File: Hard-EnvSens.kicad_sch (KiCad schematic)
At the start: 58 parts, among them J1 TYPE-C-31-M-12, J2 Conn_01x04_Socket, J3 Conn_02x02_Odd_Even, J4 Conn_01x04_Pin, Q1 SS8050, Q2 SS8050, SW1 SW_Push, SW3 SW_Push, U1 LD1117S33TR_SOT223, U2 ESP32-C6-WROOM-1, U4 VEML7700-TR, U5 DPS368, U6 SGP41-D-R4, U7 SHT40-AD1B-R2, U8 AS7341-DLGT, U9 TPS79318DBVTG4

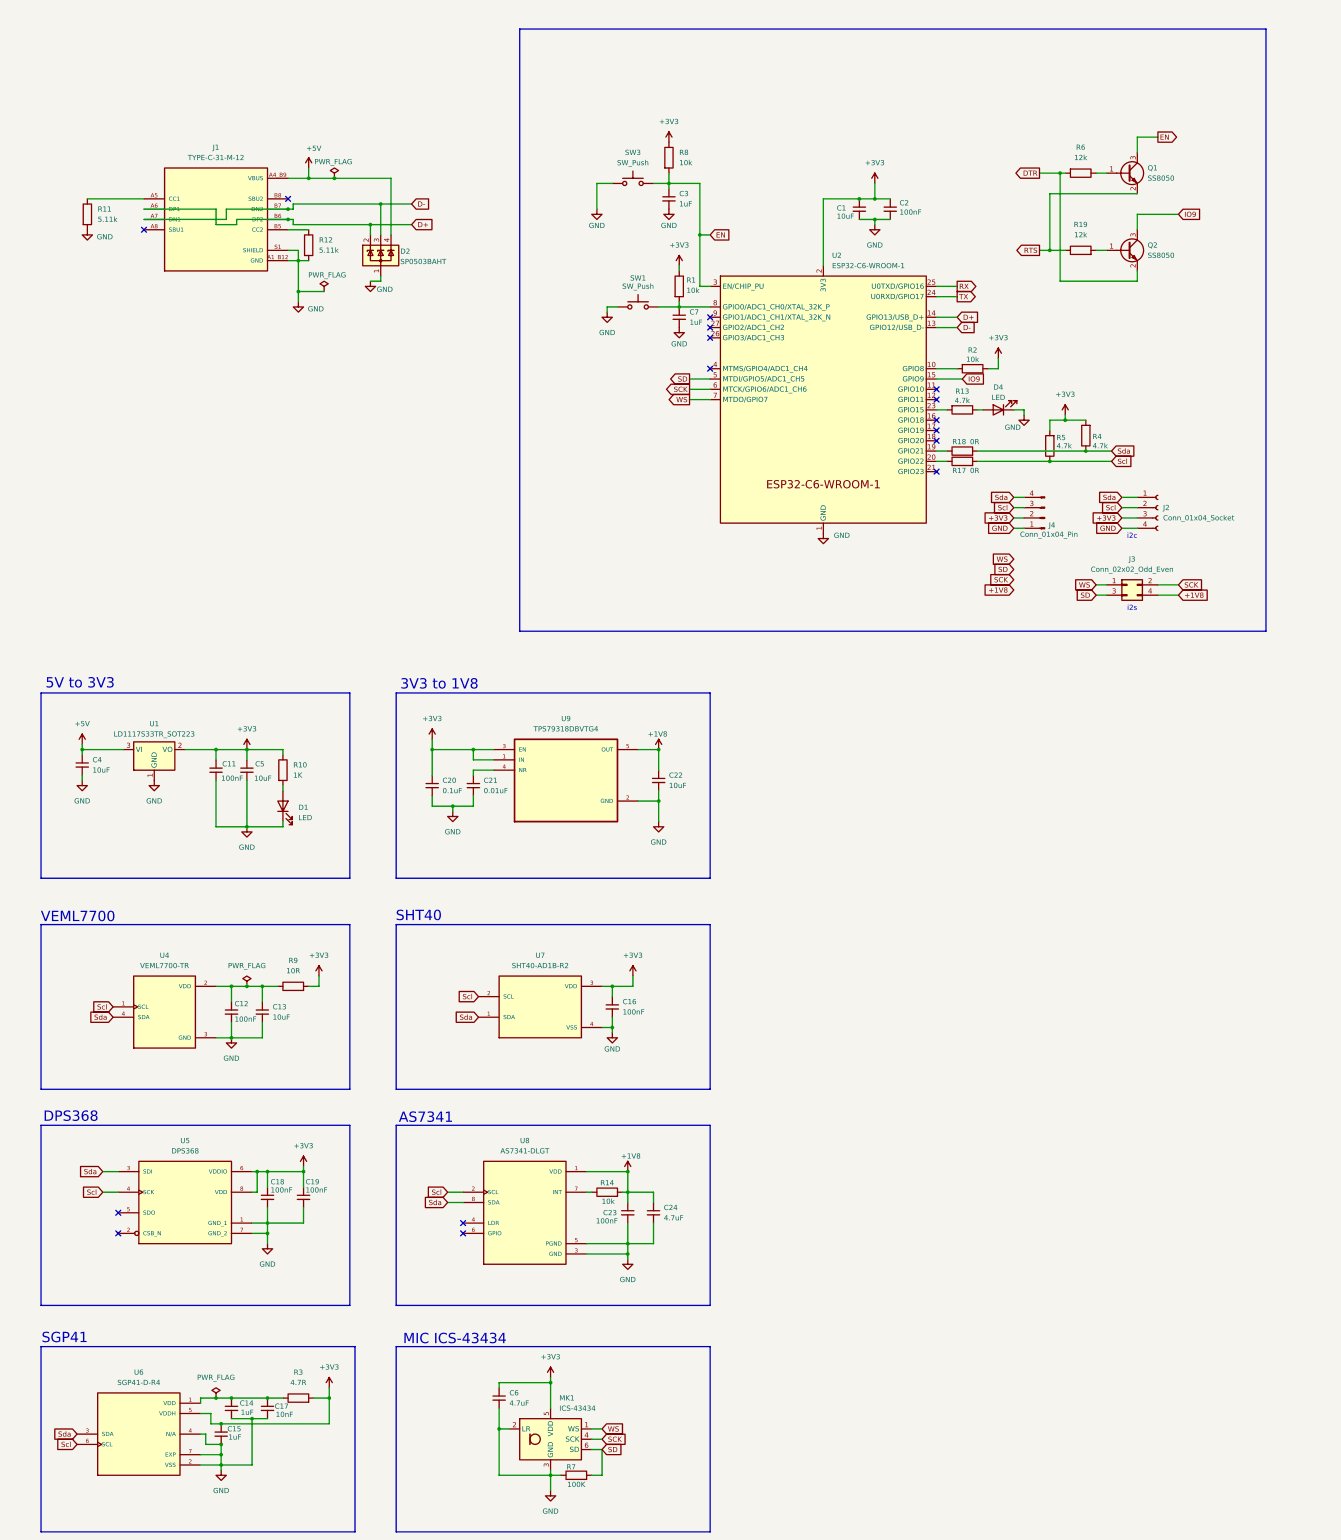
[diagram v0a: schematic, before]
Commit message: Full connected board, no charger
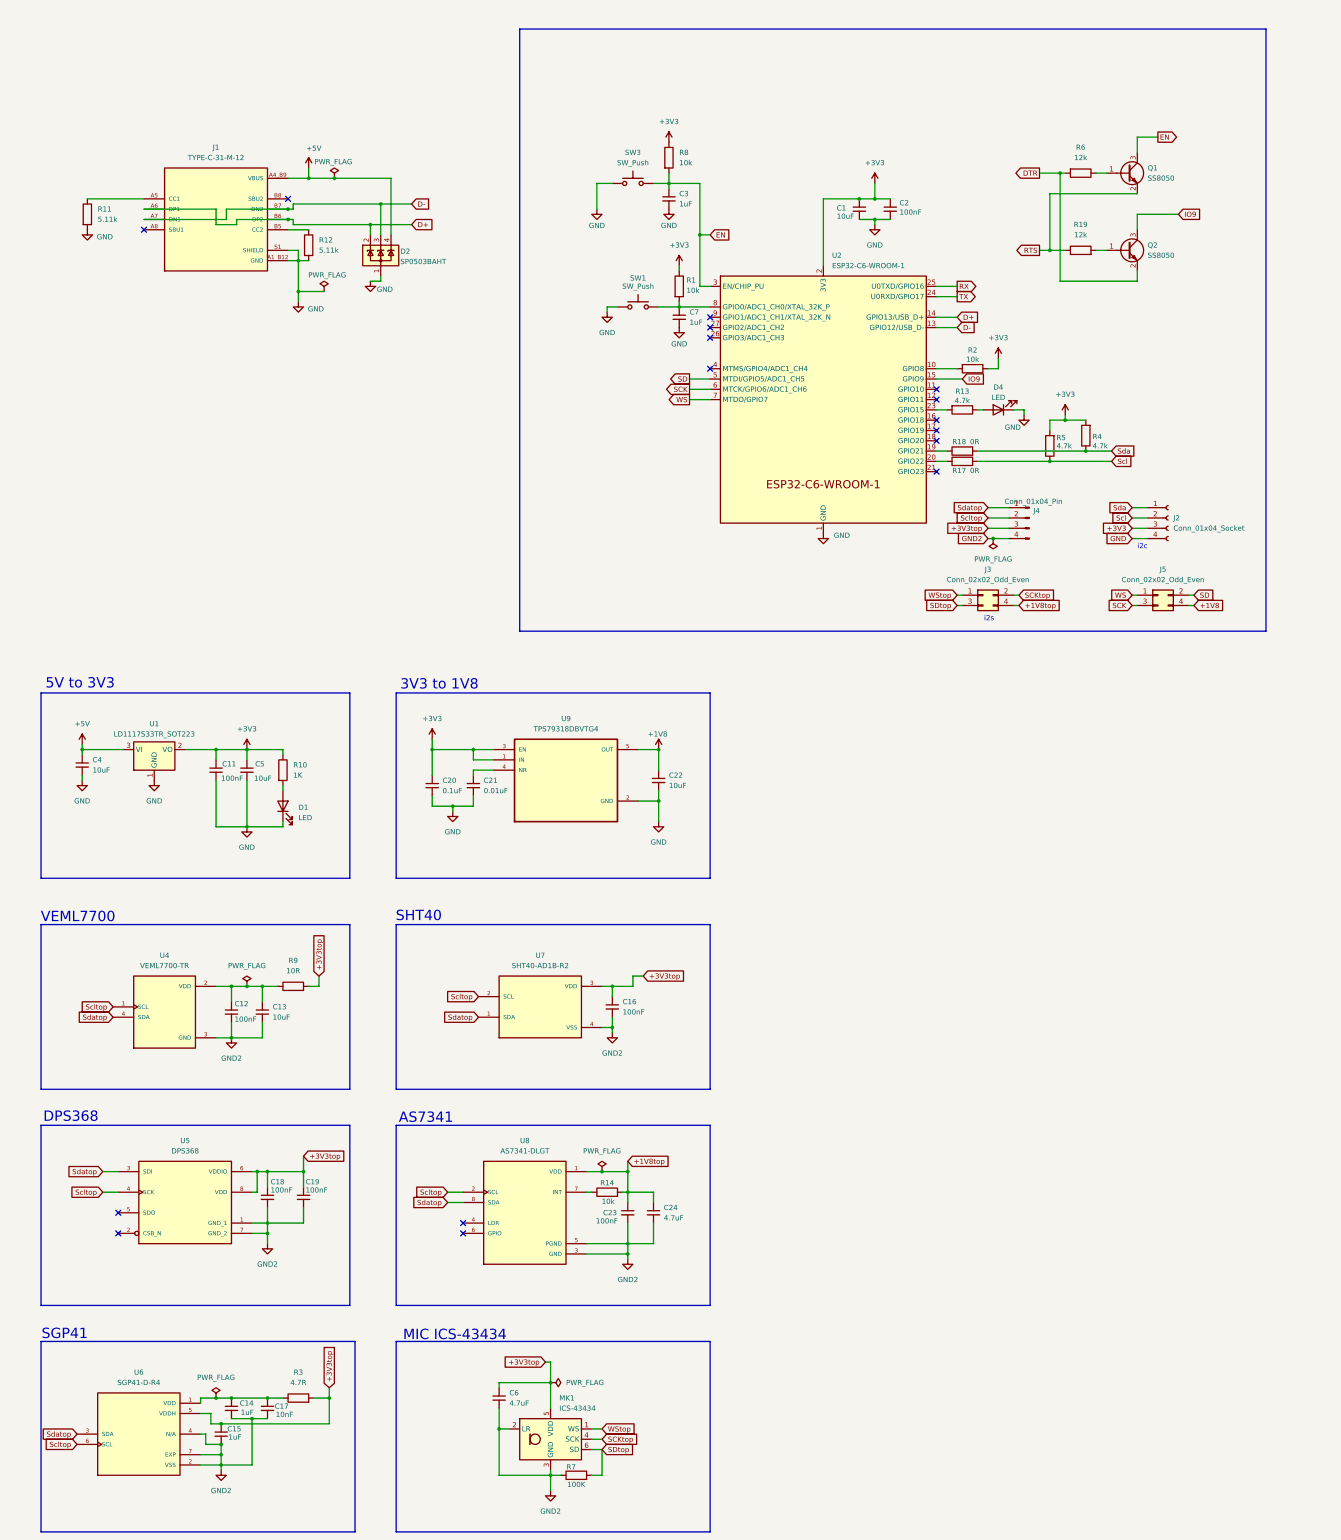
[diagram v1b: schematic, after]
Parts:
- added J5: Conn_02x02_Odd_Even, Connector_PinSocket_2.54mm:PinSocket_2x02_P2.54mm_Vertical, symbol Connector_Generic:Conn_02x02_Odd_Even
- J3: footprint Connector_PinSocket_2.54mm:PinSocket_2x02_P2.54mm_Vertical -> Connector_PinHeader_2.54mm:PinHeader_2x02_P2.54mm_Vertical
- J4: footprint (none) -> Connector_PinHeader_2.54mm:PinHeader_1x04_P2.54mm_Vertical
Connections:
- net +1V8: now also J5.4 (Pin_4); no longer C23.1, C24.1, J3.4 (Pin_4), R14.2, U8.1 (VDD)
- net +3V3: no longer C15.1, C16.1, C18.1, C19.1, C6.1, J4.2 (Pin_2), MK1.5 (VDD), R3.2, R9.2, U5.6 (VDDIO), U5.8 (VDD), U6.5 (VDDH), U7.3 (VDD)
- net GND: no longer C12.2, C13.2, C14.2, C15.2, C16.2, C17.2, C18.2, C19.2, C23.2, C24.2, C6.2, J4.1 (Pin_1), MK1.2 (LR), MK1.3 (GND), R7.1, U4.3 (GND), U5.1 (GND_1), U5.7 (GND_2), U6.2 (VSS), U6.4 (N/A), U6.7 (EXP), U7.4 (VSS), U8.3 (GND), U8.5 (PGND)
- net SCK: now also J5.3 (Pin_3); no longer J3.2 (Pin_2), MK1.4 (SCK)
- net SD: now also J5.2 (Pin_2); no longer J3.3 (Pin_3), MK1.6 (SD), R7.2
- net Scl: no longer J4.3 (Pin_3), U4.1 (SCL), U5.4 (SCK), U6.6 (SCL), U7.2 (SCL), U8.2 (SCL)
- net Sda: no longer J4.4 (Pin_4), U4.4 (SDA), U5.3 (SDI), U6.3 (SDA), U7.1 (SDA), U8.8 (SDA)
- net WS: now also J5.1 (Pin_1); no longer J3.1 (Pin_1), MK1.1 (WS)
- new net +1V8top: C23.1, C24.1, J3.4 (Pin_4), R14.2, U8.1 (VDD)
- new net +3V3top: C15.1, C16.1, C18.1, C19.1, C6.1, J4.3 (Pin_3), MK1.5 (VDD), R3.2, R9.2, U5.6 (VDDIO), U5.8 (VDD), U6.5 (VDDH), U7.3 (VDD)
- new net GND2: C12.2, C13.2, C14.2, C15.2, C16.2, C17.2, C18.2, C19.2, C23.2, C24.2, C6.2, J4.4 (Pin_4), MK1.2 (LR), MK1.3 (GND), R7.1, U4.3 (GND), U5.1 (GND_1), U5.7 (GND_2), U6.2 (VSS), U6.4 (N/A), U6.7 (EXP), U7.4 (VSS), U8.3 (GND), U8.5 (PGND)
- new net SCKtop: J3.2 (Pin_2), MK1.4 (SCK)
- new net SDtop: J3.3 (Pin_3), MK1.6 (SD), R7.2
- new net Scltop: J4.2 (Pin_2), U4.1 (SCL), U5.4 (SCK), U6.6 (SCL), U7.2 (SCL), U8.2 (SCL)
- new net Sdatop: J4.1 (Pin_1), U4.4 (SDA), U5.3 (SDI), U6.3 (SDA), U7.1 (SDA), U8.8 (SDA)
- new net WStop: J3.1 (Pin_1), MK1.1 (WS)
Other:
- moved on the sheet: J2, J3, J4

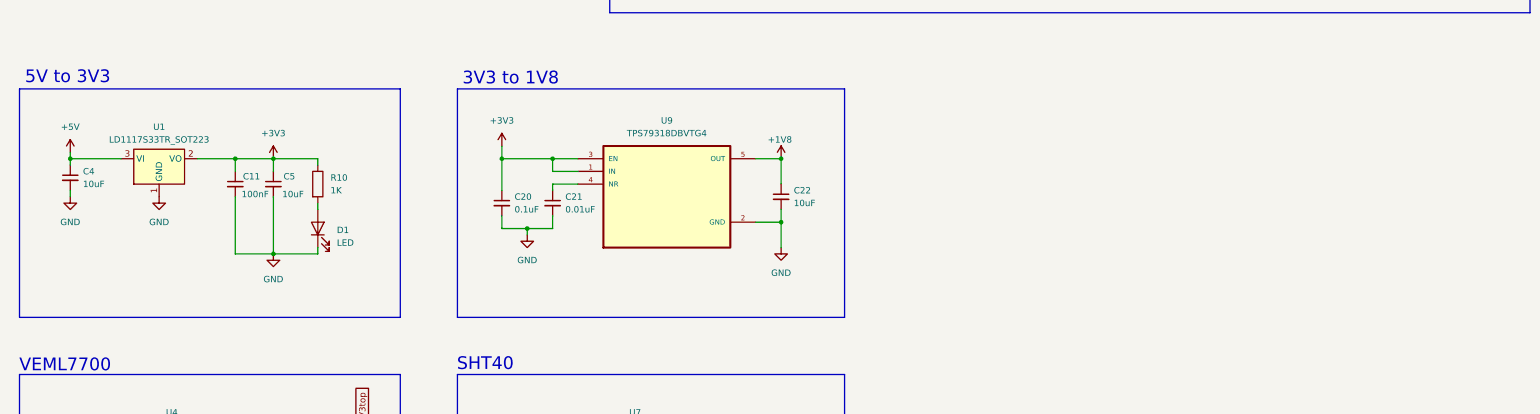
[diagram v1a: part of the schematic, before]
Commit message: Baterry charger + giroscope
Magnetometer not connected
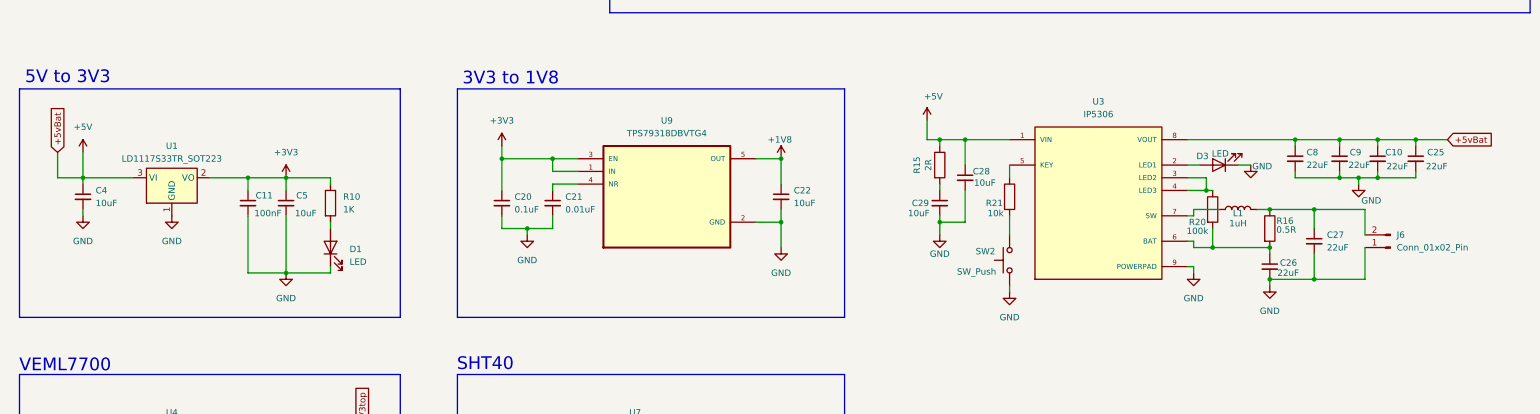
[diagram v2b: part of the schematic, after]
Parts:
- added C10, C25, C26, C27, C8, C9: 22uF, Capacitor_SMD:C_0603_1608Metric, symbol Device:C_Small
- added C28, C29: 10uF, Capacitor_SMD:C_0603_1608Metric, symbol Device:C_Small
- added D3: LED, LED_SMD:LED_0603_1608Metric, symbol Device:LED
- added J6: Conn_01x02_Pin, Connector_PinHeader_2.54mm:PinHeader_1x02_P2.54mm_Vertical, symbol Connector:Conn_01x02_Pin
- added L1: 1uH, Inductor_SMD:L_TechFuse_SL0630, symbol Device:L
- added R15: 2R, Resistor_SMD:R_0603_1608Metric, symbol Device:R
- added R16: 0.5R, Resistor_SMD:R_0603_1608Metric, symbol Device:R
- added R20: 100k, Resistor_SMD:R_0603_1608Metric, symbol Device:R
- added R21: 10k, Resistor_SMD:R_0603_1608Metric, symbol Device:R
- added SW2: SW_Push, Biblioteca_Kicad:SW_3-1437565-0, symbol Switch:SW_Push
- added U3: IP5306, libs:SOP127P600X165-9N, symbol IP5306:IP5306
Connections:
- net +5V: now also C10.1, C25.1, C28.1, C8.1, C9.1, R15.1, U3.1 (VIN), U3.8 (VOUT)
- net GND: now also C10.2, C25.2, C26.2, C27.2, C28.2, C29.2, C8.2, C9.2, D3.1 (K), J6.1 (Pin_1), SW2.1, U3.9 (POWERPAD)
- new net: C27.1, J6.2 (Pin_2), L1.2, R16.1
- new net: L1.1, U3.7 (SW)
- new net: R21.1, U3.5 (KEY)
- new net: R21.2, SW2.2
- new net: C29.1, R15.2
- new net: R20.1, U3.3 (LED2), U3.4 (LED3)
- new net: C26.1, R16.2, R20.2, U3.6 (BAT)
- new net: D3.2 (A), U3.2 (LED1)
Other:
- moved on the sheet: C11, C4, C5, D1, R10, U1
